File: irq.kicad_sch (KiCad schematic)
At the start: 8 parts, among them U1 74LS85, U11 74HCT00, U18 74LS148, U2 74HCT574, U20 74HCT574, U5 74HCT02, U8 74LS04

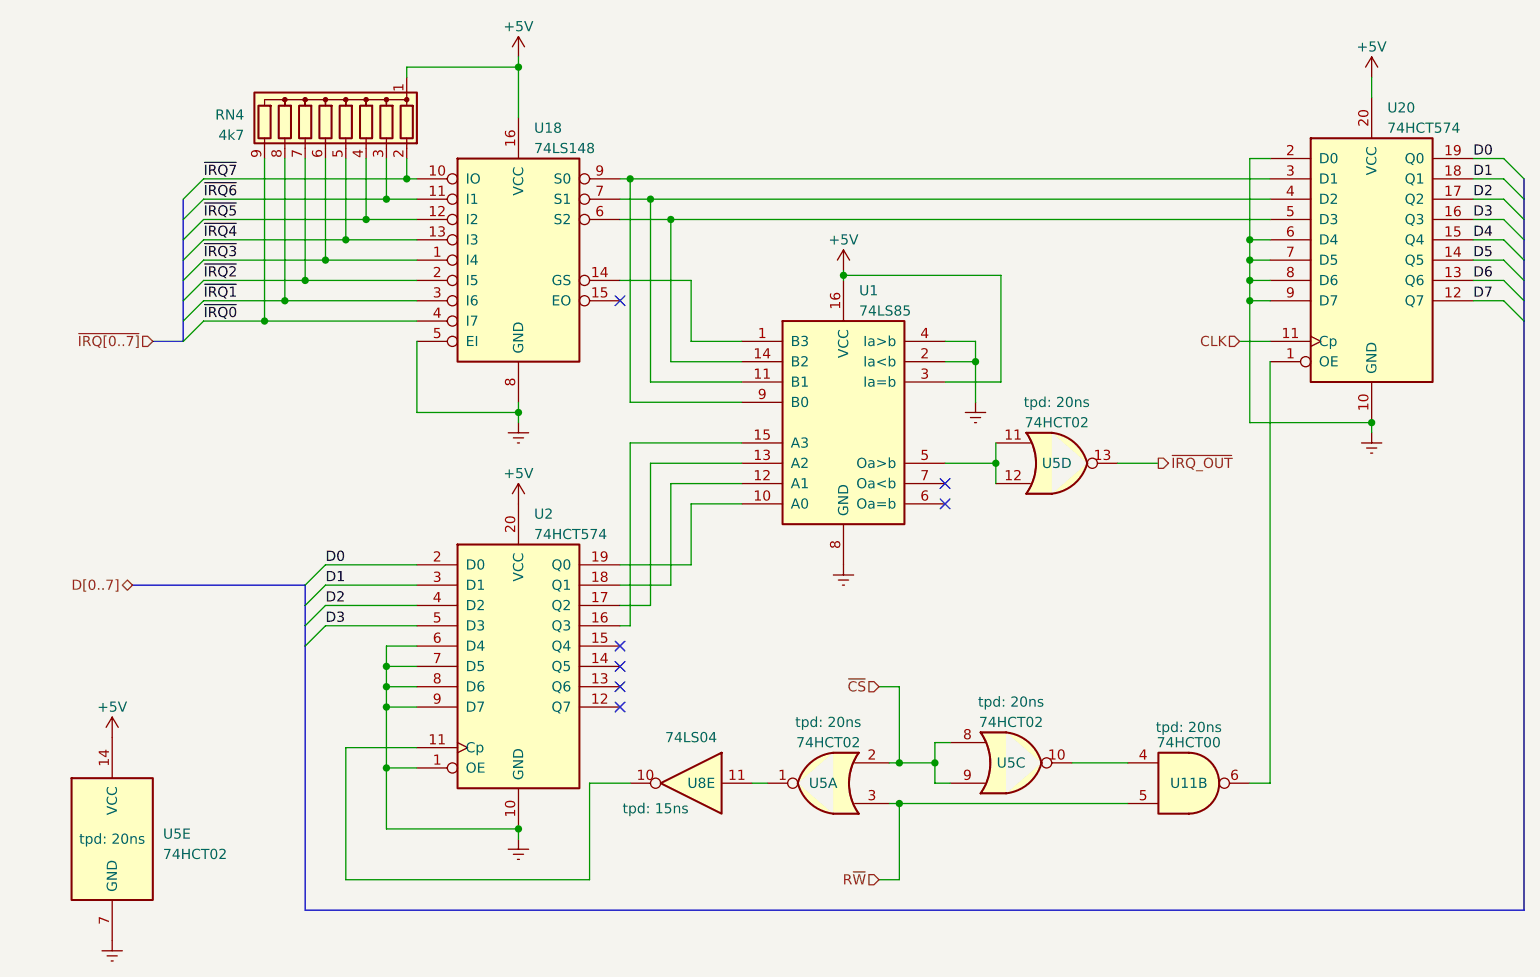
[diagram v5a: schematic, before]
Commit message: adjust timings to fast IC for address decoding
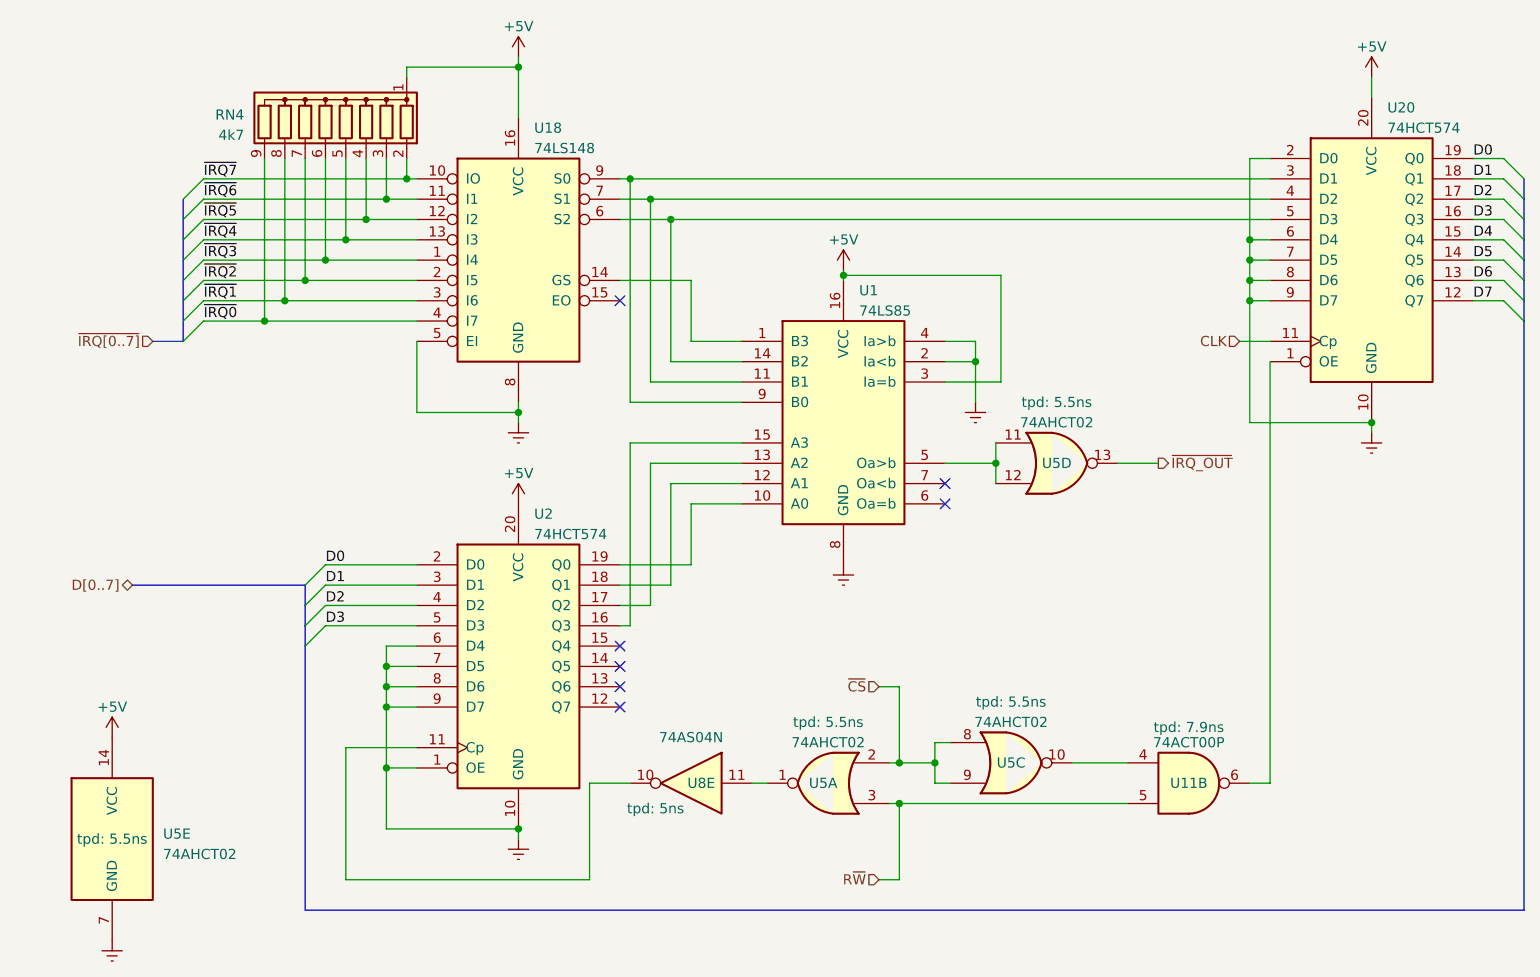
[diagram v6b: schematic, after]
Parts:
- U11: value 74HCT00 -> 74ACT00P; tpd 20ns -> 7.9ns
- U5: value 74HCT02 -> 74AHCT02; tpd 20ns -> 5.5ns
- U8: value 74LS04 -> 74AS04N; tpd 15ns -> 5ns
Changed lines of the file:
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@@
       (effects (font (size 1.27 1.27)))
     )
-    (property "Value" "74HCT02" (at 146.05 67.31 0)
+    (property "Value" "74AHCT02" (at 146.05 67.31 0)
       (effects (font (size 1.27 1.27)))
     )
@@
       (effects (font (size 1.27 1.27)) hide)
     )
-    (property "Datasheet" "http://www.ti.com/lit/gpn/sn74hct02" (at 146.05 72.39 0)
-      (effects (font (size 1.27 1.27)) hide)
-    )
-    (property "tpd" "20ns" (at 146.05 64.77 0) (show_name)
+    (property "Datasheet" "https://assets.nexperia.com/documents/data-sheet/74AHC_AHCT02.pdf" (at 146.05 72.39 0)
+      (effects (font (size 1.27 1.27)) hide)
+    )
+    (property "tpd" "5.5ns" (at 146.05 64.77 0) (show_name)
       (effects (font (size 1.27 1.27)))
     )
@@
       (effects (font (size 1.27 1.27)))
     )
-    (property "Value" "74HCT00" (at 162.5517 107.315 0)
+    (property "Value" "74ACT00P" (at 162.5517 107.315 0)
       (effects (font (size 1.27 1.27)))
     )
@@
       (effects (font (size 1.27 1.27)) hide)
     )
-    (property "Datasheet" "http://www.ti.com/lit/gpn/sn74hct00" (at 162.56 112.395 0)
-      (effects (font (size 1.27 1.27)) hide)
-    )
-    (property "tpd" "20ns" (at 162.56 105.41 0) (show_name)
+    (property "Datasheet" "https://toshiba.semicon-storage.com/info/TC74ACT00P_datasheet_en_20220525.pdf?did=3200&prodName=TC74ACT00P" (at 162.56 112.395 0)
+      (effects (font (size 1.27 1.27)) hide)
+    )
+    (property "tpd" "7.9ns" (at 162.56 105.41 0) (show_name)
       (effects (font (size 1.27 1.27)))
     )
@@
       (effects (font (size 1.27 1.27)))
     )
-    (property "Value" "74HCT02" (at 140.335 104.775 0)
+    (property "Value" "74AHCT02" (at 140.335 104.775 0)
       (effects (font (size 1.27 1.27)))
     )
@@
       (effects (font (size 1.27 1.27)) hide)
     )
-    (property "Datasheet" "http://www.ti.com/lit/gpn/sn74hct02" (at 140.335 109.855 0)
-      (effects (font (size 1.27 1.27)) hide)
-    )
-    (property "tpd" "20ns" (at 140.335 102.235 0) (show_name)
+    (property "Datasheet" "https://assets.nexperia.com/documents/data-sheet/74AHC_AHCT02.pdf" (at 140.335 109.855 0)
+      (effects (font (size 1.27 1.27)) hide)
+    )
+    (property "tpd" "5.5ns" (at 140.335 102.235 0) (show_name)
       (effects (font (size 1.27 1.27)))
     )
@@
       (effects (font (size 1.27 1.27)) (justify left))
     )
-    (property "Value" "74HCT02" (at 34.29 121.285 0)
+    (property "Value" "74AHCT02" (at 34.29 121.285 0)
       (effects (font (size 1.27 1.27)) (justify left))
     )
@@
       (effects (font (size 1.27 1.27)) hide)
     )
-    (property "Datasheet" "http://www.ti.com/lit/gpn/sn74hct02" (at 27.94 119.38 0)
-      (effects (font (size 1.27 1.27)) hide)
-    )
-    (property "tpd" "20ns" (at 27.94 119.38 0) (show_name)
+    (property "Datasheet" "https://assets.nexperia.com/documents/data-sheet/74AHC_AHCT02.pdf" (at 27.94 119.38 0)
+      (effects (font (size 1.27 1.27)) hide)
+    )
+    (property "tpd" "5.5ns" (at 27.94 119.38 0) (show_name)
       (effects (font (size 1.27 1.27)))
     )
@@
       (effects (font (size 1.27 1.27)))
     )
-    (property "Value" "74HCT02" (at 117.475 107.315 0)
+    (property "Value" "74AHCT02" (at 117.475 107.315 0)
       (effects (font (size 1.27 1.27)))
     )
@@
       (effects (font (size 1.27 1.27)) hide)
     )
-    (property "Datasheet" "http://www.ti.com/lit/gpn/sn74hct02" (at 117.475 112.395 0)
-      (effects (font (size 1.27 1.27)) hide)
-    )
-    (property "tpd" "20ns" (at 117.475 104.775 0) (show_name)
+    (property "Datasheet" "https://assets.nexperia.com/documents/data-sheet/74AHC_AHCT02.pdf" (at 117.475 112.395 0)
+      (effects (font (size 1.27 1.27)) hide)
+    )
+    (property "tpd" "5.5ns" (at 117.475 104.775 0) (show_name)
       (effects (font (size 1.27 1.27)))
     )
@@
       (effects (font (size 1.27 1.27)))
     )
-    (property "Value" "74LS04" (at 100.33 106.68 0)
+    (property "Value" "74AS04N" (at 100.33 106.68 0)
       (effects (font (size 1.27 1.27)))
     )
@@
       (effects (font (size 1.27 1.27)) hide)
     )
-    (property "Datasheet" "http://www.ti.com/lit/gpn/sn74LS04" (at 100.33 112.395 0)
-      (effects (font (size 1.27 1.27)) hide)
-    )
-    (property "tpd" "15ns" (at 95.885 115.57 0) (show_name)
-      (effects (font (size 1.27 1.27)))
-    )
-    (pin "1")
+    (property "Datasheet" "http://www.ti.com/lit/gpn/sn74AS04" (at 100.33 112.395 0)
+      (effects (font (size 1.27 1.27)) hide)
+    )
+    (property "tpd" "5ns" (at 95.885 115.57 0) (show_name)
+      (effects (font (size 1.27 1.27)))
+    )
+    (property "Field5" "" (at 100.33 112.395 0)
+      (effects (font (size 1.27 1.27)) hide)
+    )
+    (pin "1")
